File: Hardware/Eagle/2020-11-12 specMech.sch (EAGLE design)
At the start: 86 parts, among them J1 PINHD-1X8-MOLEX-SHROUD, J2 JST-2-PIN-2B-PH-K-S(LF)(SN), J3 PINHD-1X8-MOLEX-SHROUD, J4 PINHD-1X8-MOLEX-SHROUD, J6 Molex 0022232081, J7 Lantronix XPORT, J8 Molex 0022232081, U1 MCP23008-E/SO, U10 ADS1115, U11 MCP23008-E/SO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

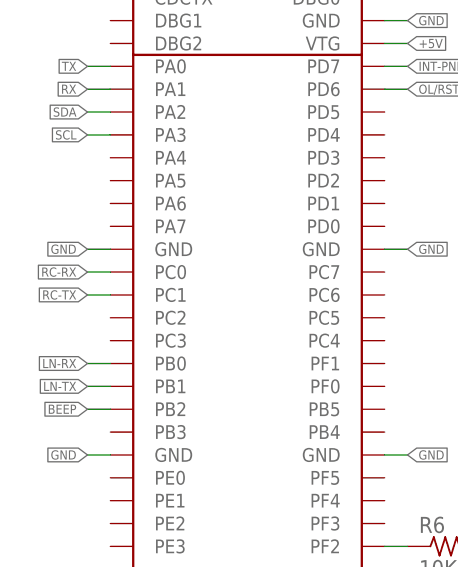
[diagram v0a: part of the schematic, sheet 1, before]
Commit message: Forced rebootack to be !<CR> EXACTLY
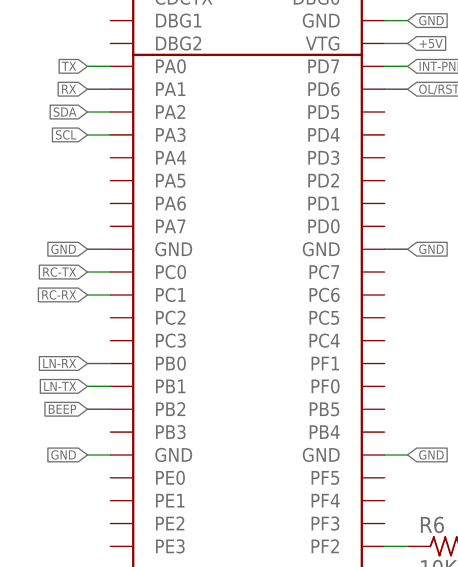
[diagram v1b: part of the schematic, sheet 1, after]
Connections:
- net RC-RX: now also CNANO1.PC1, U12.2Y; no longer CNANO1.PC0, U12.1A
- net RC-TX: now also CNANO1.PC0, U12.1A; no longer CNANO1.PC1, U12.2Y
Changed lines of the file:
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@@
 </segment>
 </net>
-<net name="RC-TX" class="0">
+<net name="RC-RX" class="0">
 <segment>
 <pinref part="CNANO1" gate="G$1" pin="PC1"/>
@@
 </segment>
 </net>
-<net name="RC-RX" class="0">
+<net name="RC-TX" class="0">
 <segment>
 <pinref part="CNANO1" gate="G$1" pin="PC0"/>
@@
 </segment>
 </net>
-<net name="RC-TX" class="0">
+<net name="RC-RX" class="0">
 <segment>
 <pinref part="U12" gate="A" pin="2Y"/>
@@
 </segment>
 </net>
-<net name="RC-RX" class="0">
+<net name="RC-TX" class="0">
 <segment>
 <pinref part="U12" gate="A" pin="1A"/>
